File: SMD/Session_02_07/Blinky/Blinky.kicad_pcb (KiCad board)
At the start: 2 copper layers, 30 x 30 mm, 15 parts, among them U1 TLC551CD‎

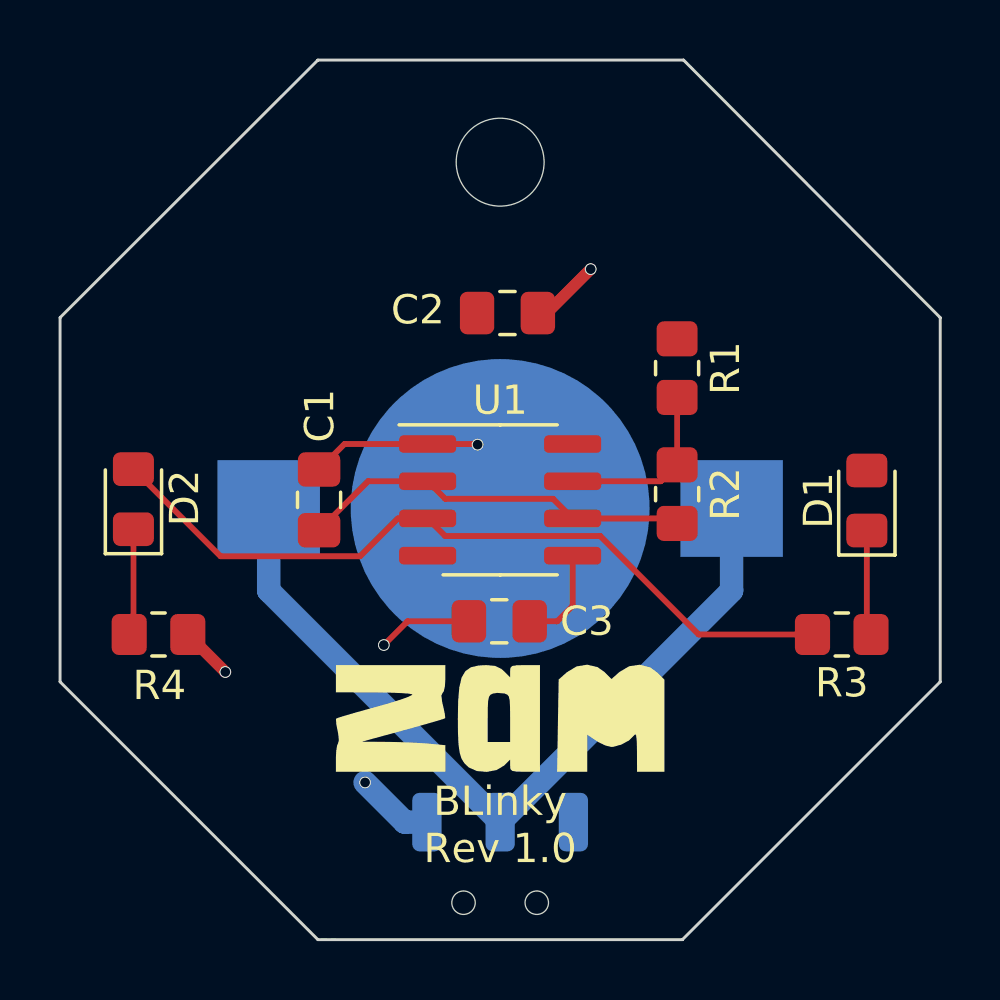
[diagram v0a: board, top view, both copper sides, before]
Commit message: Makes corrections to the design rules
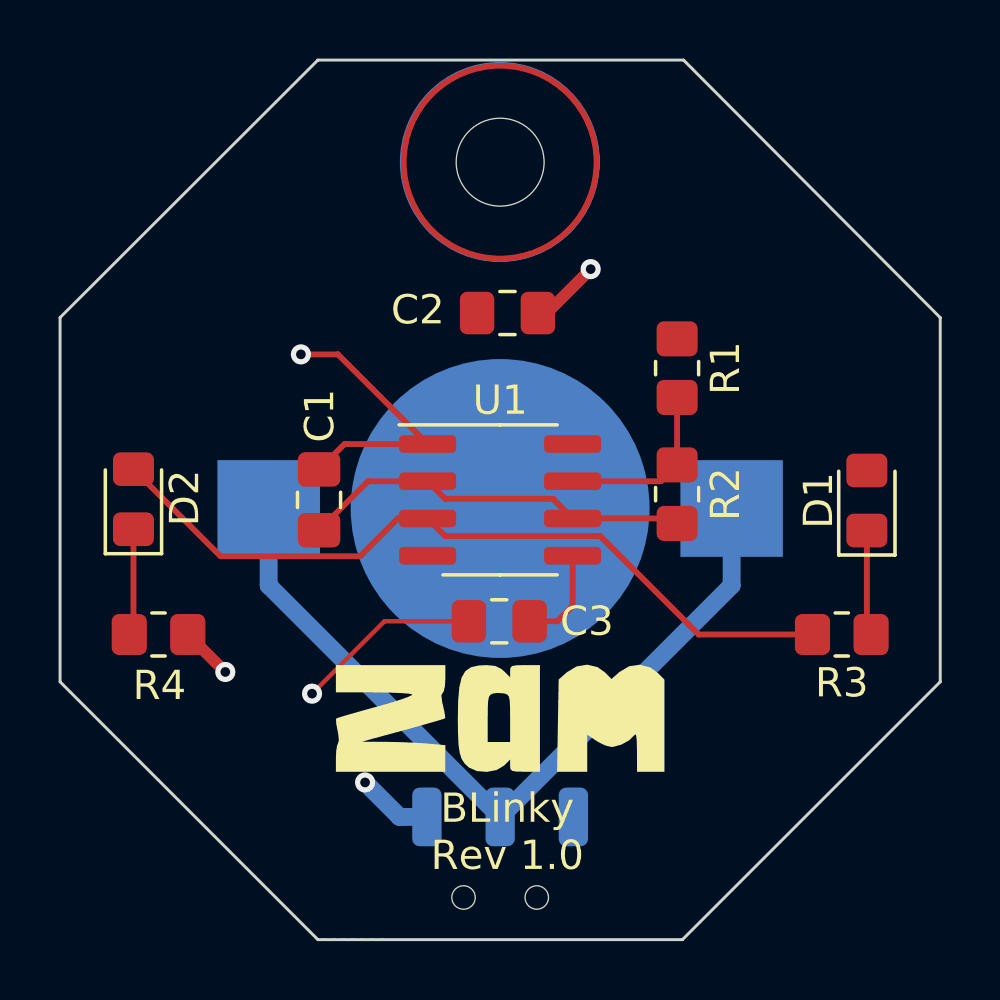
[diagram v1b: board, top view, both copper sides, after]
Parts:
- moved LG? 17.9 mm to (184.4, 45.5), turned to -135 degrees
- moved SW? 0.18 mm to (193.1, 64.5)
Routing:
- net GND: track 13.2 -> 20.3 mm
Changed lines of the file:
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@@
     (48 "B.Fab" user)
     (49 "F.Fab" user)
-    (50 "User.1" user)
-    (51 "User.2" user)
-    (52 "User.3" user)
-    (53 "User.4" user)
-    (54 "User.5" user)
-    (55 "User.6" user)
-    (56 "User.7" user)
-    (57 "User.8" user)
-    (58 "User.9" user)
+    (50 "User.1" user "Nutzer.1")
+    (51 "User.2" user "Nutzer.2")
+    (52 "User.3" user "Nutzer.3")
+    (53 "User.4" user "Nutzer.4")
+    (54 "User.5" user "Nutzer.5")
+    (55 "User.6" user "Nutzer.6")
+    (56 "User.7" user "Nutzer.7")
+    (57 "User.8" user "Nutzer.8")
+    (58 "User.9" user "Nutzer.9")
   )
   (setup
@@
   )
   (footprint "Blinky_ZAM:SSK-1202" (layer "B.Cu")
-    (at 193.05 64.6944)
+    (at 193.05 64.516401)
     (property "Datasheet" "~")
     (property "Reference" "SW?")
@@
       (effects (font (size 1 1) (thickness 0.15)) (justify mirror))
     )
-    (fp_rect (start -3.500001 1) (end 3.500001 4) (layer "B.SilkS") (width 0.1524) (fill none))
     (fp_rect (start -2 5.499999) (end -0.5 4) (layer "B.SilkS") (width 0.1524) (fill none))
+    (fp_rect (start -3.500001 1.2) (end 3.6 4) (layer "B.SilkS") (width 0.1524) (fill none))
     (fp_rect (start -3.5 5.5) (end 3.5 -1) (layer "B.CrtYd") (width 0.01) (fill none))
     (pad "" np_thru_hole circle (at -1.25 2.75) (size 0.8 0.8) (drill 0.8) (layers F&B.Cu *.Mask))
@@
   )
   (footprint "Blinky_ZAM:ZAM_LOGO_440" (layer "B.Cu")
-    (at 193.08 61.132866 180)
+    (at 184.404 45.466 -135)
     (property "Reference" "LG?")
     (property "Sheetfile" "Blinky.kicad_sch")
@@
     (property "Value" "LOGO")
     (attr board_only exclude_from_pos_files)
-    (fp_text reference "LG1" (at -0.01 -3.049999) (layer "User.1") hide
+    (fp_text reference "LG1" (at -0.01 -3.049999 45) (layer "User.1") hide
       (effects (font (size 1.524 1.524) (thickness 0.3)))
     )
-    (fp_text value "LOGO" (at 0.75 0) (layer "B.SilkS") hide
+    (fp_text value "LOGO" (at 0.75 0 45) (layer "B.SilkS") hide
       (effects (font (size 1.524 1.524) (thickness 0.3)) (justify mirror))
     )
@@
     )
   )
+  (gr_circle locked (center 193.050008 42.169994) (end 196.342013 42.169994) (layer "F.Cu") (width 0.2) (fill none))
+  (gr_circle locked (center 193.04 42.164) (end 196.351756 42.164) (layer "B.Cu") (width 0.2) (fill none))
   (gr_poly
     (pts
@@
       (xy 199.31 38.685)
     ) (layer "Edge.Cuts") (width 0.1) (fill none))
-  (gr_text "BLinky\nRev 1.0" (at 193.05 64.79) (layer "F.SilkS")
+  (gr_text "BLinky\nRev 1.0" (at 193.294 65.024) (layer "F.SilkS")
     (effects (font (size 1 1) (thickness 0.15)))
   )
-  (segment (start 193.05 64.6944) (end 185.15 56.7944) (width 0.8) (layer "B.Cu") (net 1))
-  (segment (start 193.05 64.6944) (end 200.95 56.7944) (width 0.8) (layer "B.Cu") (net 1))
-  (segment (start 200.95 56.7944) (end 200.95 53.99) (width 0.8) (layer "B.Cu") (net 1))
-  (segment (start 185.15 56.7944) (end 185.15 53.99) (width 0.8) (layer "B.Cu") (net 1))
-  (segment (start 191.9825 57.84) (end 189.89 57.84) (width 0.2) (layer "F.Cu") (net 2))
+  (segment (start 200.95 56.616401) (end 200.95 53.99) (width 0.6096) (layer "B.Cu") (net 1))
+  (segment (start 193.05 64.516401) (end 200.95 56.616401) (width 0.6096) (layer "B.Cu") (net 1))
+  (segment (start 193.05 64.516401) (end 185.15 56.616401) (width 0.6096) (layer "B.Cu") (net 1))
+  (segment (start 185.15 56.616401) (end 185.15 53.99) (width 0.6096) (layer "B.Cu") (net 1))
   (segment (start 194.3375 47.32) (end 194.64 47.32) (width 0.4) (layer "F.Cu") (net 2))
-  (segment (start 192.26 51.79) (end 192.28 51.81) (width 0.2) (layer "F.Cu") (net 2))
+  (segment (start 189.1 57.84) (end 186.63 60.31) (width 0.1524) (layer "F.Cu") (net 2))
+  (segment (start 190.575 51.79) (end 187.515 48.73) (width 0.2) (layer "F.Cu") (net 2))
+  (segment (start 191.9825 57.84) (end 189.1 57.84) (width 0.1524) (layer "F.Cu") (net 2))
   (segment (start 194.64 47.32) (end 196.14 45.82) (width 0.4) (layer "F.Cu") (net 2))
+  (segment (start 187.515 48.73) (end 186.25 48.73) (width 0.2) (layer "F.Cu") (net 2))
   (segment (start 182.39 58.29) (end 183.67 59.57) (width 0.4) (layer "F.Cu") (net 2))
   (segment (start 187.7375 51.79) (end 190.575 51.79) (width 0.2) (layer "F.Cu") (net 2))
-  (segment (start 189.89 57.84) (end 189.08 58.65) (width 0.2) (layer "F.Cu") (net 2))
-  (segment (start 190.575 51.79) (end 192.26 51.79) (width 0.2) (layer "F.Cu") (net 2))
   (segment (start 186.87 52.6575) (end 187.7375 51.79) (width 0.2) (layer "F.Cu") (net 2))
-  (via (at 189.08 58.65) (size 0.4) (drill 0.3302) (layers "F.Cu" "B.Cu") (net 2))
-  (via (at 192.28 51.81) (size 0.4) (drill 0.3302) (layers "F.Cu" "B.Cu") (net 2))
-  (via (at 183.67 59.57) (size 0.4) (drill 0.3302) (layers "F.Cu" "B.Cu") (net 2))
-  (via (at 196.14 45.82) (size 0.4) (drill 0.3302) (layers "F.Cu" "B.Cu") (net 2))
+  (via (at 196.14 45.82) (size 0.6858) (drill 0.3302) (layers "F.Cu" "B.Cu") (net 2))
+  (via (at 186.25 48.73) (size 0.6858) (drill 0.3302) (layers "F.Cu" "B.Cu") (net 2))
+  (via (at 183.67 59.57) (size 0.6858) (drill 0.3302) (layers "F.Cu" "B.Cu") (net 2))
+  (via (at 186.63 60.31) (size 0.6858) (drill 0.3302) (layers "F.Cu" "B.Cu") (net 2))
   (segment (start 190.575 53.06) (end 188.5425 53.06) (width 0.2) (layer "F.Cu") (net 3))
   (segment (start 198.92 54.33) (end 199.09 54.5) (width 0.2) (layer "F.Cu") (net 3))
@@
   (segment (start 191.17452 53.65952) (end 194.85452 53.65952) (width 0.2) (layer "F.Cu") (net 3))
   (segment (start 195.525 54.33) (end 198.92 54.33) (width 0.2) (layer "F.Cu") (net 3))
-  (via (at 188.44 63.34) (size 0.4) (drill 0.3302) (layers "F.Cu" "B.Cu") (net 4))
-  (segment (start 189.7944 64.6944) (end 188.44 63.34) (width 0.8) (layer "B.Cu") (net 4))
-  (segment (start 190.55 64.6944) (end 189.7944 64.6944) (width 0.8) (layer "B.Cu") (net 4))
+  (via (at 188.44 63.34) (size 0.6858) (drill 0.3302) (layers "F.Cu" "B.Cu") (net 4))
+  (segment (start 189.616401 64.516401) (end 188.44 63.34) (width 0.6096) (layer "B.Cu") (net 4))
+  (segment (start 190.55 64.516401) (end 189.616401 64.516401) (width 0.6096) (layer "B.Cu") (net 4))
   (segment (start 195.525 57.315) (end 195.525 55.6) (width 0.2) (layer "F.Cu") (net 5))
   (segment (start 194.0575 57.84) (end 195 57.84) (width 0.2) (layer "F.Cu") (net 5))

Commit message: Corrections to the switch footprint
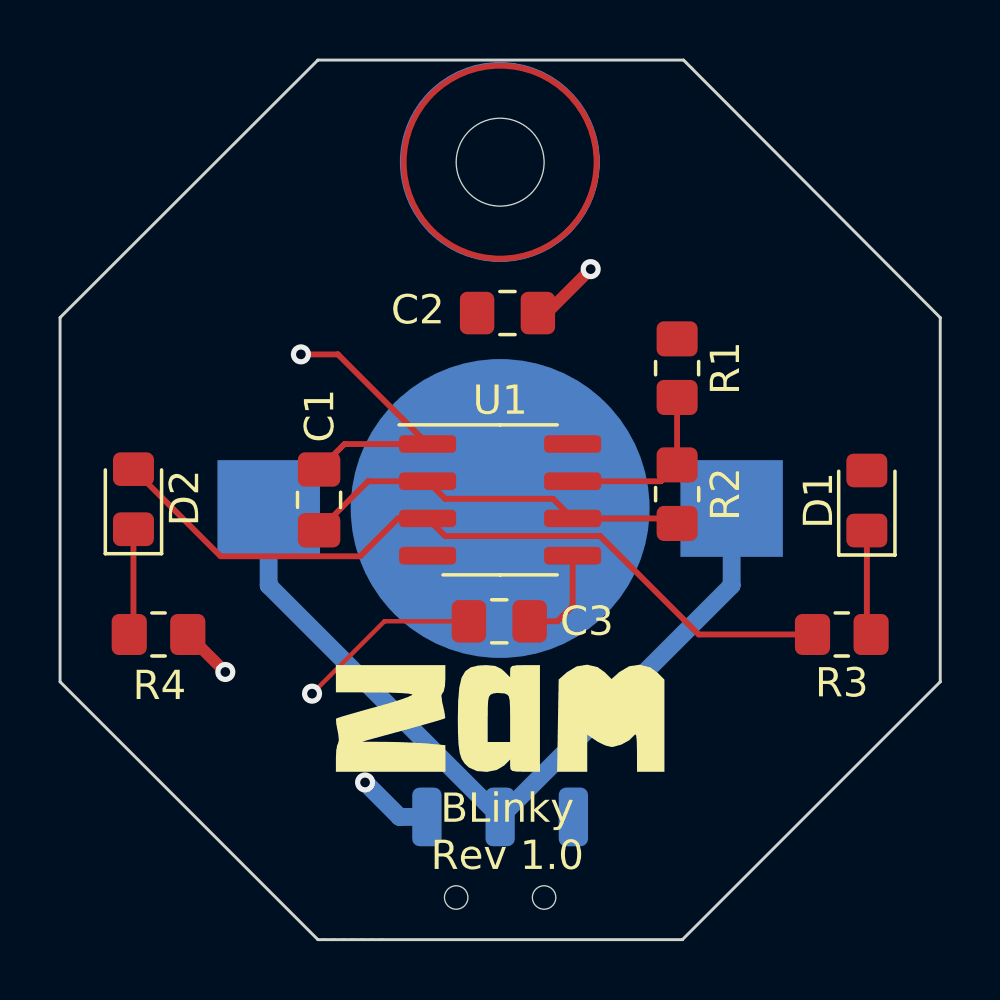
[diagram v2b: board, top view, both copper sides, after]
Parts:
- turned BT1 to 0 degrees
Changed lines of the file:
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@@
       (effects (font (size 1 1) (thickness 0.15)) (justify mirror))
     )
+    (fp_rect (start -3.500001 1.1) (end 3.500001 4) (layer "B.SilkS") (width 0.1524) (fill none))
     (fp_rect (start -2 5.499999) (end -0.5 4) (layer "B.SilkS") (width 0.1524) (fill none))
-    (fp_rect (start -3.500001 1.2) (end 3.6 4) (layer "B.SilkS") (width 0.1524) (fill none))
     (fp_rect (start -3.5 5.5) (end 3.5 -1) (layer "B.CrtYd") (width 0.01) (fill none))
-    (pad "" np_thru_hole circle (at -1.25 2.75) (size 0.8 0.8) (drill 0.8) (layers F&B.Cu *.Mask))
-    (pad "" np_thru_hole circle (at 1.25 2.75) (size 0.8 0.8) (drill 0.8) (layers F&B.Cu *.Mask))
+    (pad "" np_thru_hole circle (at -1.5 2.75) (size 0.8 0.8) (drill 0.8) (layers F&B.Cu *.Mask))
+    (pad "" np_thru_hole circle (at 1.5 2.75) (size 0.8 0.8) (drill 0.8) (layers F&B.Cu *.Mask))
     (pad "1" smd roundrect (at -2.5 0) (size 1 2) (layers "B.Cu" "B.Paste" "B.Mask") (roundrect_rratio 0.25)
       (net 4 "/VCC") (pinfunction "A") (pintype "passive"))
@@
   )
   (footprint "Battery:BatteryHolder_Keystone_3000_1x12mm" (layer "B.Cu")
-    (at 193.05 53.99 180)
+    (at 193.05 53.99)
     (descr "http://www.keyelco.com/product-pdf.cfm?p=777")
     (tags "Keystone type 3000 coin cell retainer")
@@
     (fp_arc (start -5.378013 -5.447558) (mid -4.942443 -5.378013) (end -4.6 -5.1) (layer "B.Fab") (width 0.1))
     (fp_arc (start 5.3 -5.45) (mid 6.239949 -5.019238) (end 6.6 -4.05) (layer "B.Fab") (width 0.1))
-    (pad "1" smd rect (at 7.9 0 180) (size 3.5 3.3) (layers "B.Cu" "B.Paste" "B.Mask")
+    (pad "1" smd rect (at 7.9 0) (size 3.5 3.3) (layers "B.Cu" "B.Paste" "B.Mask")
       (net 1 "Net-(BT1-Pad1)") (pinfunction "+") (pintype "passive"))
-    (pad "1" smd rect (at -7.9 0 180) (size 3.5 3.3) (layers "B.Cu" "B.Paste" "B.Mask")
+    (pad "1" smd rect (at -7.9 0) (size 3.5 3.3) (layers "B.Cu" "B.Paste" "B.Mask")
       (net 1 "Net-(BT1-Pad1)") (pinfunction "+") (pintype "passive"))
-    (pad "2" smd circle (at 0 0 180) (size 10.2 10.2) (layers "B.Cu" "B.Mask")
+    (pad "2" smd circle (at 0 0) (size 10.2 10.2) (layers "B.Cu" "B.Mask")
       (net 2 "GND") (pinfunction "-") (pintype "passive"))
     (model "${KICAD6_3DMODEL_DIR}/Battery.3dshapes/BatteryHolder_Keystone_3000_1x12mm.wrl"
